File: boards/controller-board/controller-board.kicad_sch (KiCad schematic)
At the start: 169 parts, among them J1 Conn_01x02, J2 Conn_01x02, J3 Conn_01x02, J4 Conn_01x02, J5 Conn_01x03, J6 Conn_01x02, Q1 SQS460EN, Q2 DGD0216, SW1 EG1271, U1 CAT4201, U10 CAT4201, U11 CAT4201, U12 CAT4201, U13 CAT4201, U14 CAT4201, U15 CAT4201, U17 CAT4201, U18 CAT4201, U2 PocketBeagle, U3 LTC3624, U4 CAT4201, U5 CAT4201, U6 CAT4201, U7 MCP4728, U8 ADS1015IRUGR, U9 ADS1015IRUGR

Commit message: Fixed schematic overflow
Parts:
- D22, D23: value ELUA3535OGB-P6070U23240500-VD1M -> NP
- D47, D48: value ELUC3535NUB-P7085Q15070100-S22Q -> NP
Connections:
- no-connect marks 2 -> 63
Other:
- note added: "OreSat Solar Simulator Controller Board v1.1"
- note removed: "OreSat Solar Simulator Controller Board v1.0"

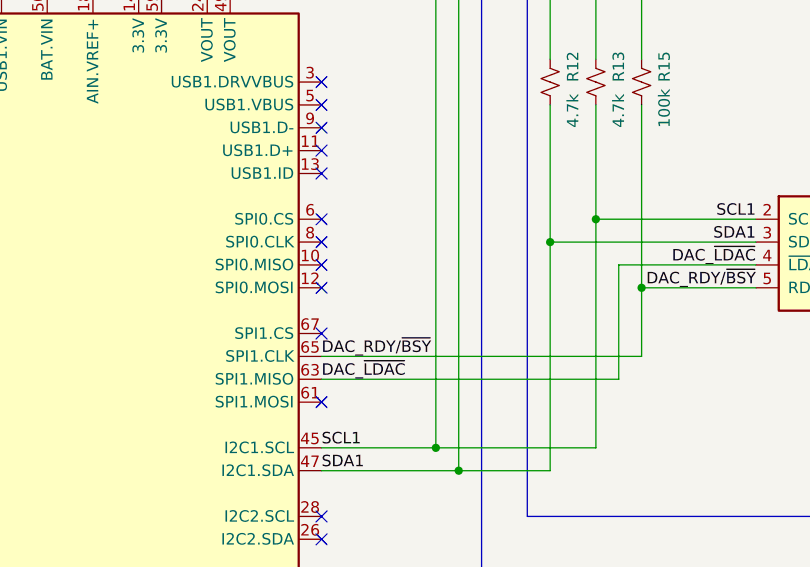
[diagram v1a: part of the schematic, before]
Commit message: Fixed library paths on controller board
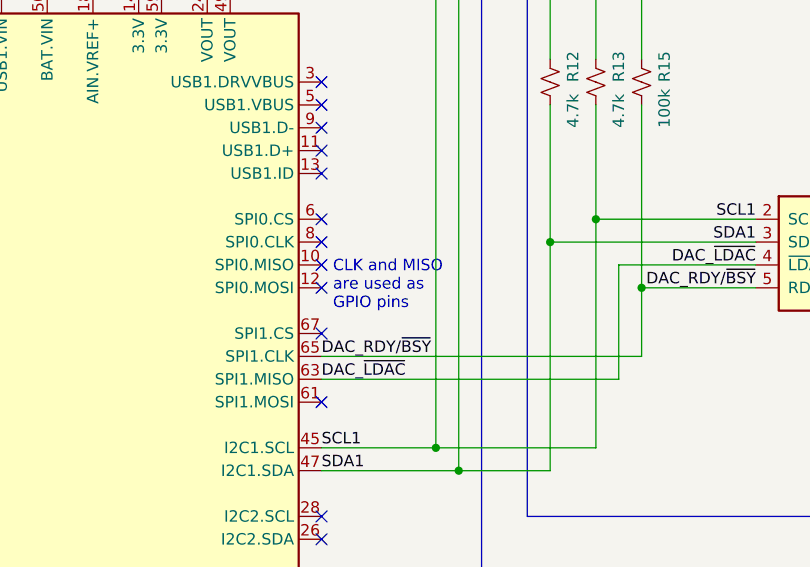
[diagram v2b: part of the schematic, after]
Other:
- note added: "CLK and MISO are used as GPIO pins"
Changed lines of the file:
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@@
     (effects (font (size 2.032 2.032)) (justify left bottom))
+  )
+  (text "CLK and MISO\nare used as\nGPIO pins" (at 227.33 154.94 0)
+    (effects (font (size 1.27 1.27)) (justify left bottom))
   )
   (text "Blue LED Channel" (at 469.9 83.82 0)

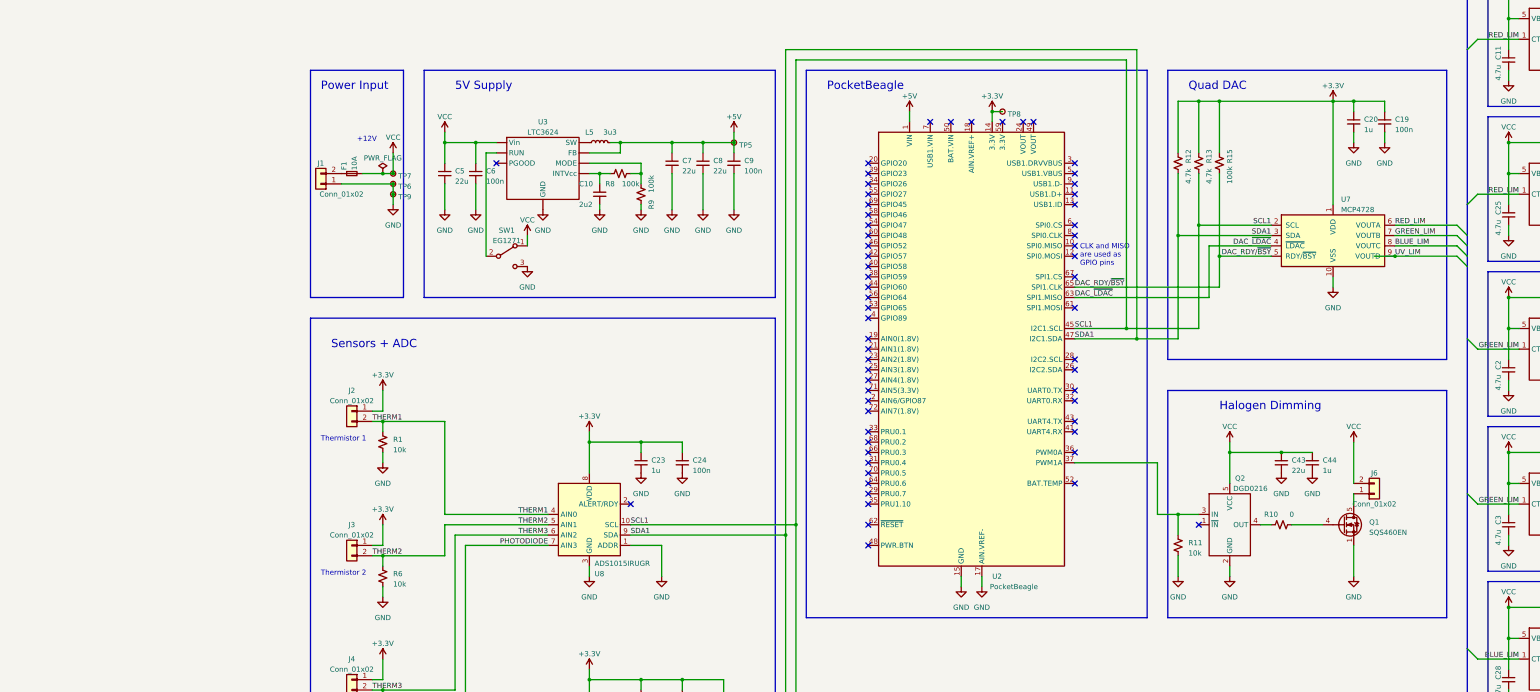
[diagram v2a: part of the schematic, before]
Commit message: added notes to schematic
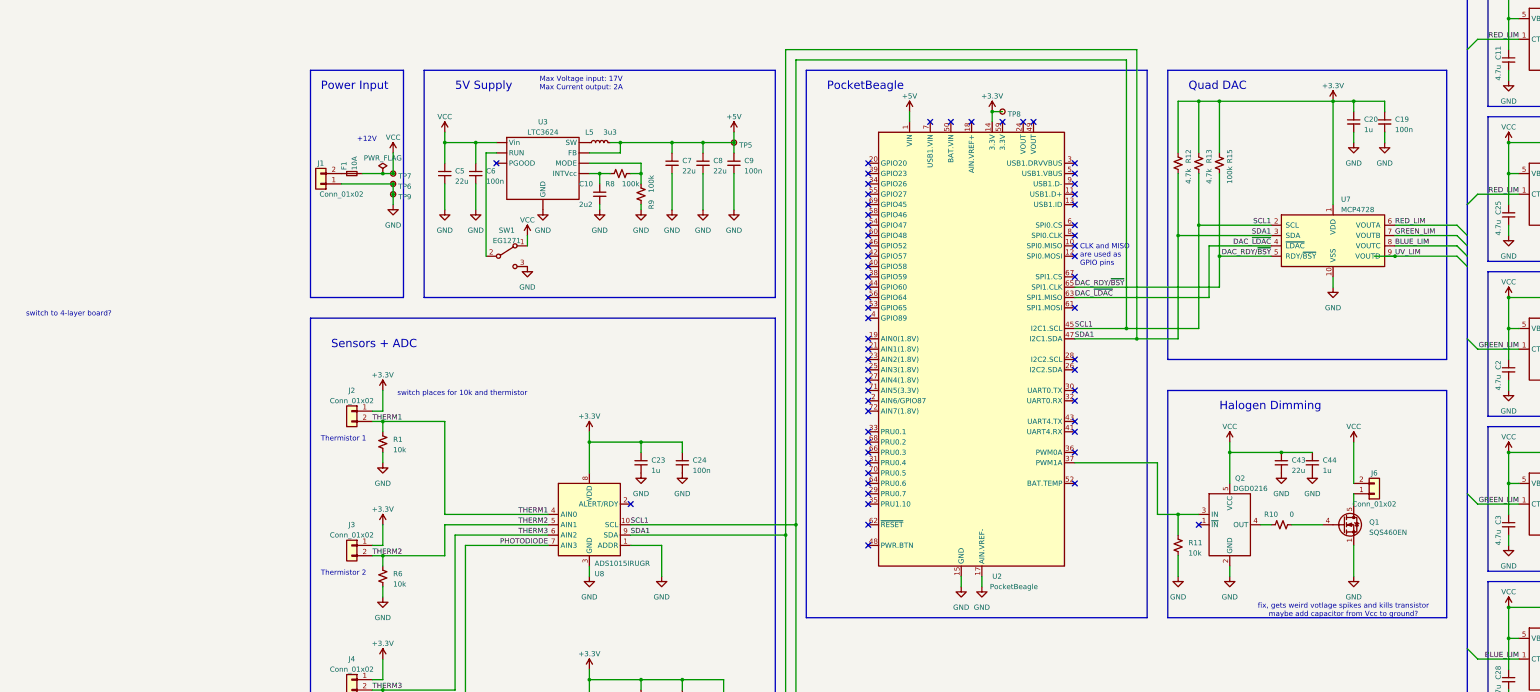
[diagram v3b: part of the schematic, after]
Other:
- note added: "Max Voltage input: 17V Max Current output: 2A"
- note added: "fix, gets weird votlage spikes and kills transistor maybe add capacitor from Vcc to ground?"
- note added: "switch places for 10k and thermistor"
- note added: "switch to 4-layer board?"

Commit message: finished schematic
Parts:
- removed Q1: SQS460EN, Package_SO:Vishay_PowerPAK_1212-8_Single, symbol Transistor_FET:SiS454DN
- removed Q2: DGD0216, Package_TO_SOT_SMD:TSOT-23-5, symbol oresat-ics:DGD0216
- removed TP8: TestPoint-MinTH, oresat-misc:TestPoint-MinTH, symbol oresat-misc:TestPoint-MinTH
- removed U2: PocketBeagle, Module:BeagleBoard_PocketBeagle, symbol MCU_Module:PocketBeagle
- added C51: C_Small, symbol Device:C_Small
- added Q1: Goford_G11S_20V_11A, Package_SO:SOP-8_3.9x4.9mm_P1.27mm, symbol oresat-transistors:Goford_G11S_20V_11A
- added Q2: PMV45EN, symbol Device:Q_NMOS_GSD
- added R23: 1k, symbol Device:R_Small_US
- added U16: RPi_Pico, oresat-misc:RPi_Pico_TH, symbol oresat-misc:RPi_Pico
- U3: footprint Package_DFN_QFN:DFN-8-1EP_3x3mm_P0.5mm_EP1.65x2.38mm -> oresat-ics:DFN-8-1EP_3x3mm_P0.5mm_EP1.65x2.38mm_ThermalVias0.3mm
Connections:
- net +3.3V: now also U16.36 (3V3)
- net +5V: now also U16.39 (VSYS)
- net DAC_RDY/~{BSY}: now also U16.21 (GPIO16)
- net DAC_~{LDAC}: now also U16.22 (GPIO17)
- net GND: now also C51.2, Q1.1 (S), Q2.2 (S), U16.13 (GND), U16.18 (GND), U16.23 (GND), U16.28 (GND), U16.3 (GND), U16.33 (AGND), U16.38 (GND), U16.42 (GND)
- net SCL1: now also U16.32 (GPIO27_ADC1)
- net SDA1: now also U16.31 (GPIO26_ADC0)
- net VCC: now also R23.1
- net at R11.1: now also Q2.1 (G), U16.34 (GPIO28_ADC2)
- net at J6.1 (Pin_1): now also Q1.5
- net at R10.1: now also Q2.3 (D), R23.2
- net at R10.2: now also C51.1, Q1.4 (G)
- no-connect marks 63 -> 31
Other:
- note added: "Input from SS"
- note added: "Output to SS"
- note removed: "PocketBeagle"

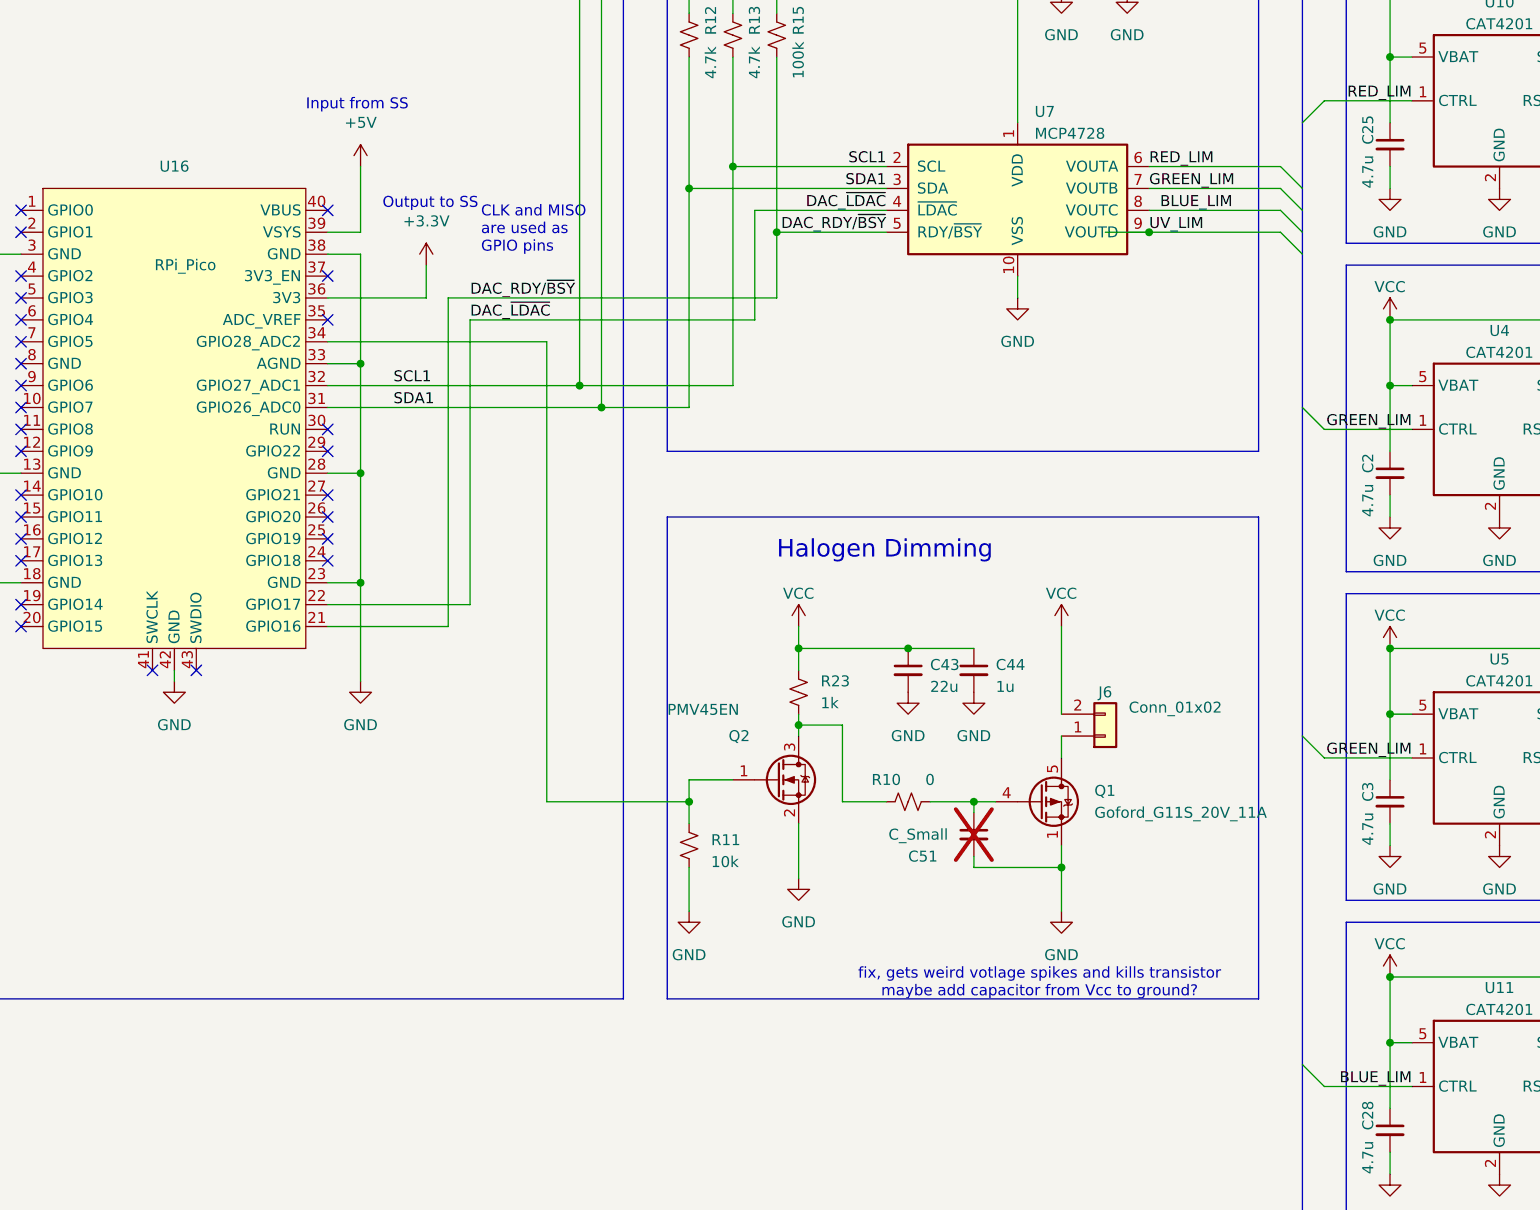
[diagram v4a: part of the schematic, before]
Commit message: fixed footprints for some components
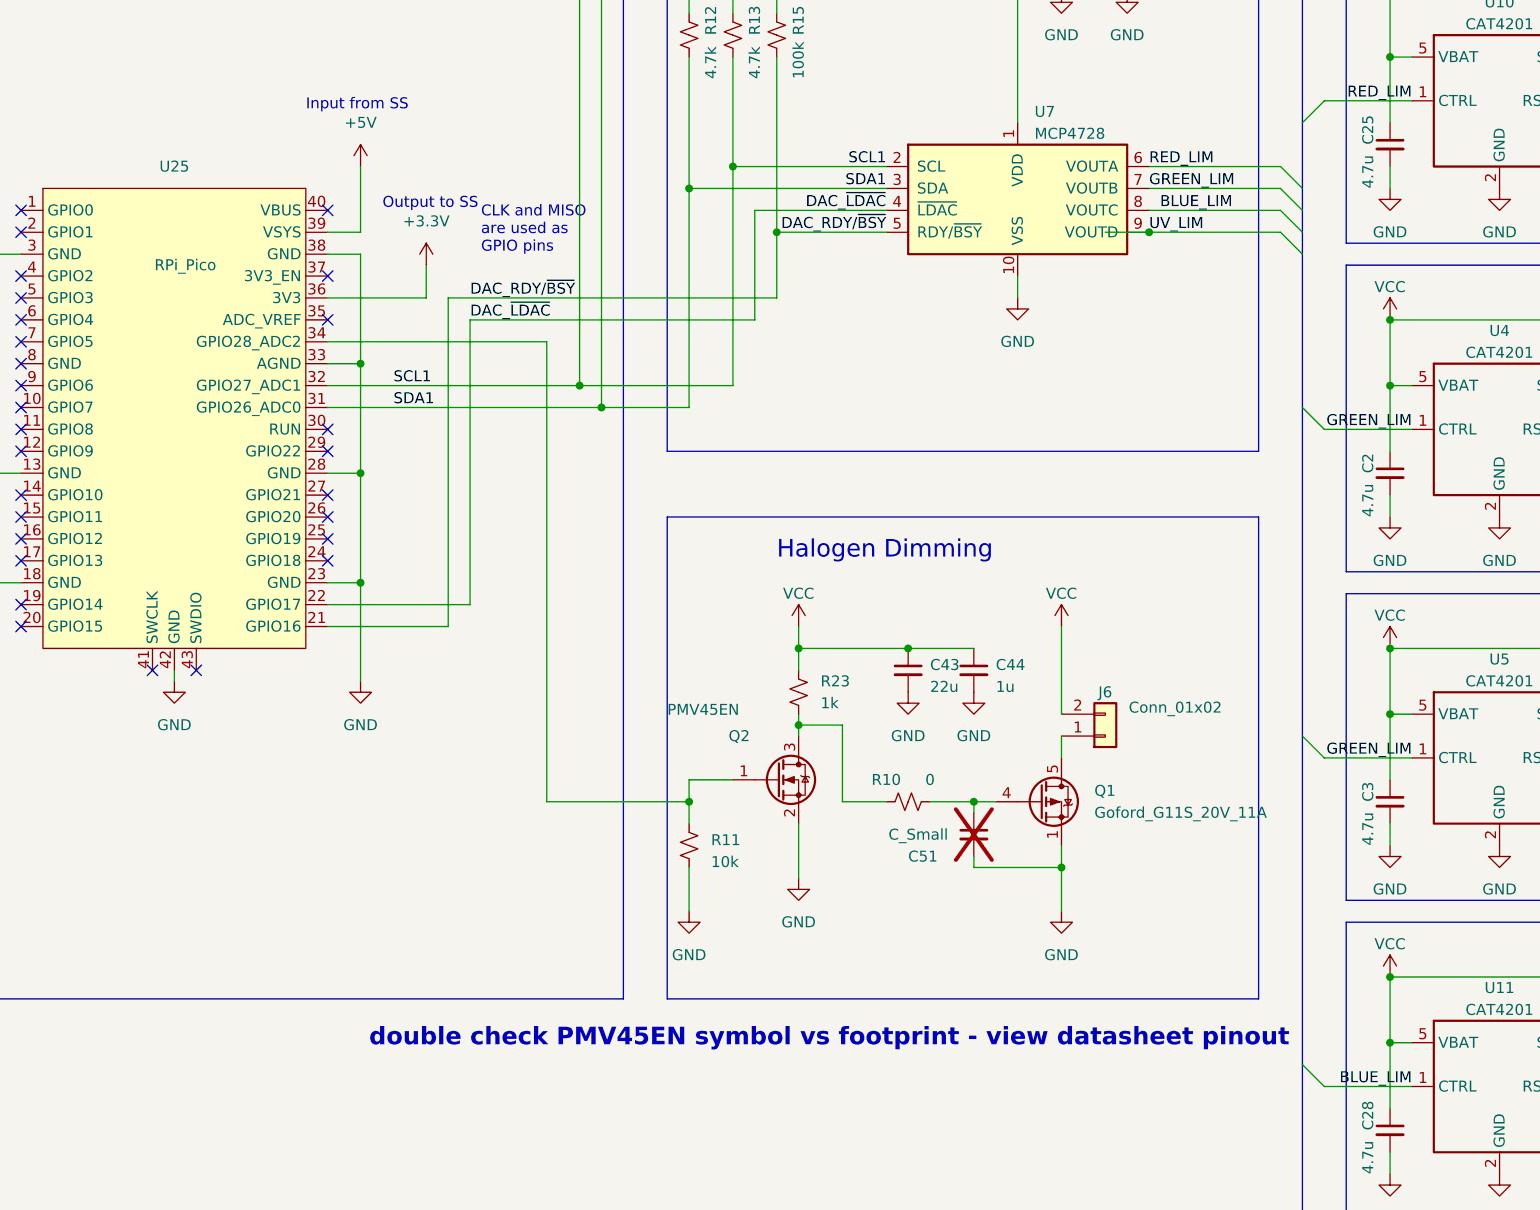
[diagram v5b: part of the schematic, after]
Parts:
- Q2: footprint (none) -> Package_TO_SOT_SMD:SOT-23-3
- R23: footprint (none) -> Resistor_SMD:R_0603_1608Metric
- renumbered U16 to U25
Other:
- note added: "double check PMV45EN symbol vs footprint - view datasheet pinout"
- note removed: "fix, gets weird votlage spikes and kills transistor maybe add capacitor from Vcc to ground?"
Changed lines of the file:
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@@
 		)
 	)
-	(text "fix, gets weird votlage spikes and kills transistor\nmaybe add capacitor from Vcc to ground?"
+	(text "double check PMV45EN symbol vs footprint - view datasheet pinout "
 		(exclude_from_sim no)
-		(at 292.1 239.522 0)
+		(at 267.716 245.872 0)
 		(effects
 			(font
-				(size 1.27 1.27)
+				(size 2.032 2.032)
+				(thickness 0.4064)
+				(bold yes)
+				(color 255 9 47 1)
 			)
 		)
@@
 		(dnp no)
 		(fields_autoplaced yes)
-		(property "Reference" "U16"
+		(property "Reference" "U25"
 			(at 191.77 144.78 0)
 			(effects
@@
 			(project "controller-board"
 				(path "/ab186ba7-5fdc-41ea-88f4-a283b73948bc"
-					(reference "U16")
+					(reference "U25")
 					(unit 1)
 				)
@@
 			)
 		)
-		(property "Footprint" ""
+		(property "Footprint" "Package_TO_SOT_SMD:SOT-23-3"
 			(at 266.7 213.36 0)
 			(effects
@@
 			)
 		)
-		(property "Datasheet" "~"
+		(property "Datasheet" "https://assets.nexperia.com/documents/data-sheet/PMV45EN2.pdf"
 			(at 261.62 215.9 0)
 			(effects
@@
 			)
 		)
-		(property "Footprint" ""
+		(property "Footprint" "Resistor_SMD:R_0603_1608Metric"
 			(at 264.16 205.74 0)
 			(effects
